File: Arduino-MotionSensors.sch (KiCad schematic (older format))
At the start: 22 parts, among them IC1 ATMEGA328-P, K1 CONN_3, K2 CONN_3, K3 RELAY_1RT, K4 RELAY_1RT, P1 CONN_2, P2 CONN_2, P3 CONN_2, Q1 2N222, Q2 2N222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

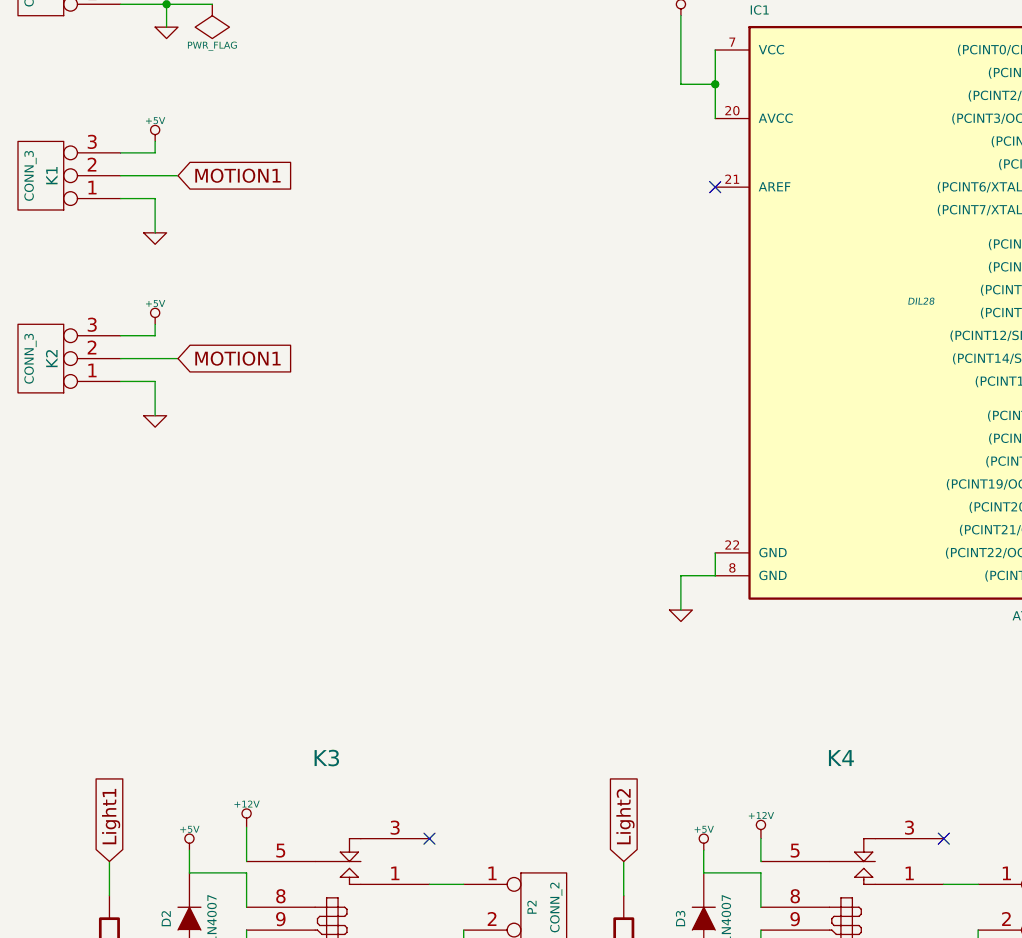
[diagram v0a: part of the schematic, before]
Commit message: Renamed a connectors to p#, and r-orded relays.
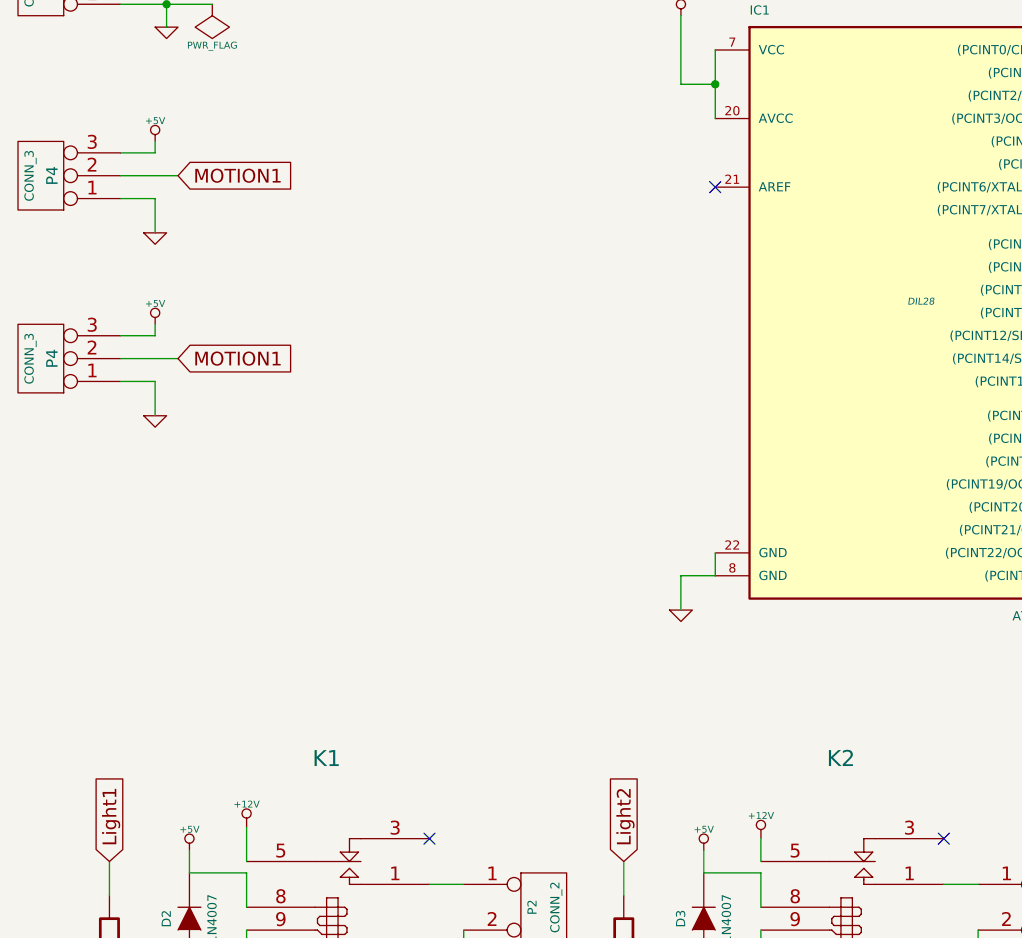
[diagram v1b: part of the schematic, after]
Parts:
- renumbered K3 to K1, K4 to K2, K1 to P4, K2 to P4
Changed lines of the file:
@@
 Sheet 1 1
 Title "Arduino Motion Sensor"
-Date "10 mar 2014"
+Date "18 apr 2014"
 Rev ""
 Comp "Mark Kromis"
@@
 	2750 6000 2750 6150
 $Comp
-L RELAY_1RT K3
+L RELAY_1RT K1
 U 1 1 531CB06A
 P 2200 5650
-F 0 "K3" H 2150 6050 70  0000 C CNN
+F 0 "K1" H 2150 6050 70  0000 C CNN
 F 1 "RELAY_1RT" H 2350 5150 70  0000 C CNN
 F 2 "~" H 2200 5650 60  0000 C CNN
@@
 	5000 6000 5000 6150
 $Comp
-L RELAY_1RT K4
+L RELAY_1RT K2
 U 1 1 531CB1B4
 P 4450 5650
-F 0 "K4" H 4400 6050 70  0000 C CNN
+F 0 "K2" H 4400 6050 70  0000 C CNN
 F 1 "RELAY_1RT" H 4600 5150 70  0000 C CNN
 F 2 "~" H 4450 5650 60  0000 C CNN
@@
 	1450 1950 1450 2050
 $Comp
-L CONN_3 K1
+L CONN_3 P4
 U 1 1 531CB7C5
 P 900 2700
-F 0 "K1" V 850 2700 50  0000 C CNN
+F 0 "P4" V 850 2700 50  0000 C CNN
 F 1 "CONN_3" V 950 2700 40  0000 C CNN
 F 2 "" H 900 2700 60  0000 C CNN
@@
 	1400 2800 1250 2800
 $Comp
-L CONN_3 K2
+L CONN_3 P4
 U 1 1 531CB8D3
 P 900 3500
-F 0 "K2" V 850 3500 50  0000 C CNN
+F 0 "P4" V 850 3500 50  0000 C CNN
 F 1 "CONN_3" V 950 3500 40  0000 C CNN
 F 2 "" H 900 3500 60  0000 C CNN
